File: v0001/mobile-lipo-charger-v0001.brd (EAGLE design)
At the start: 82.9 x 108.6 mm, 31 parts, among them IC2 STM32F401VBT, SW1 DHT-4235A

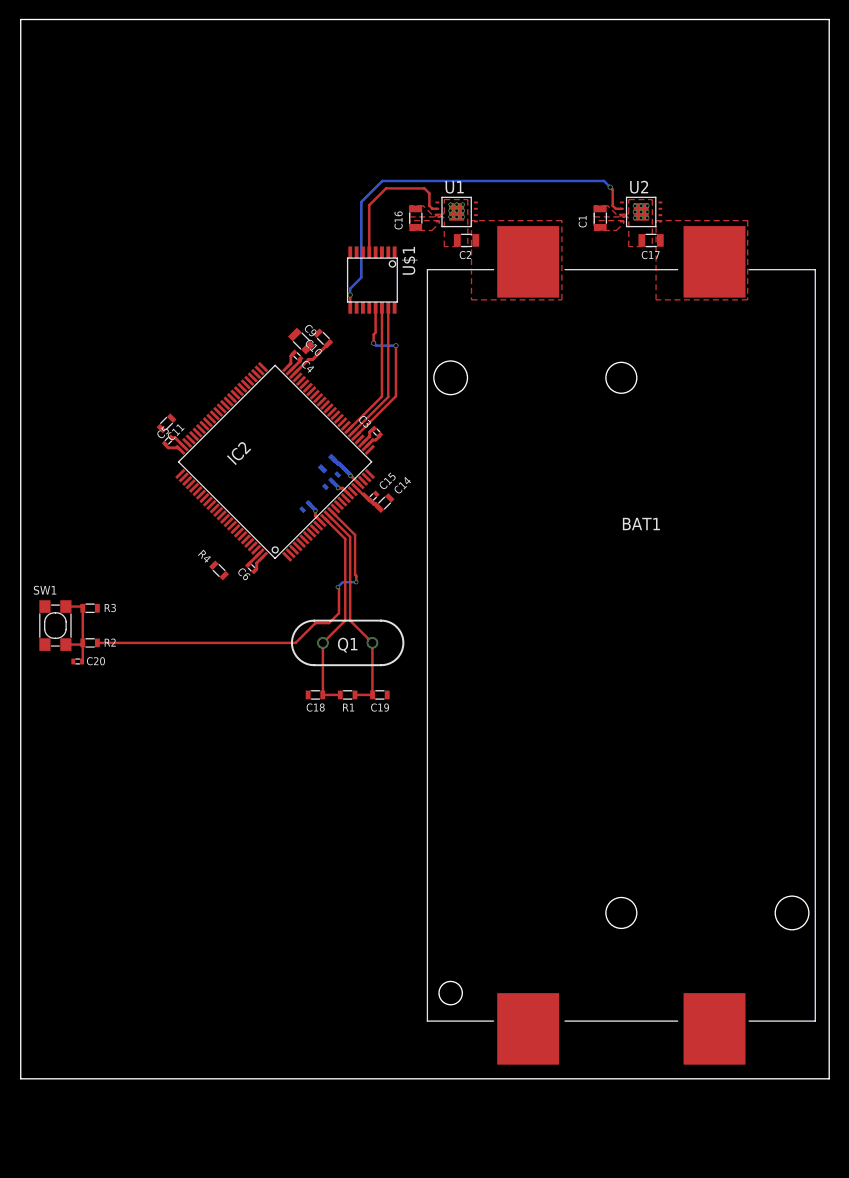
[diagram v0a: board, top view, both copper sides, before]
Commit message: Minor Changes
Made minor changes to the polygons for the charger chips
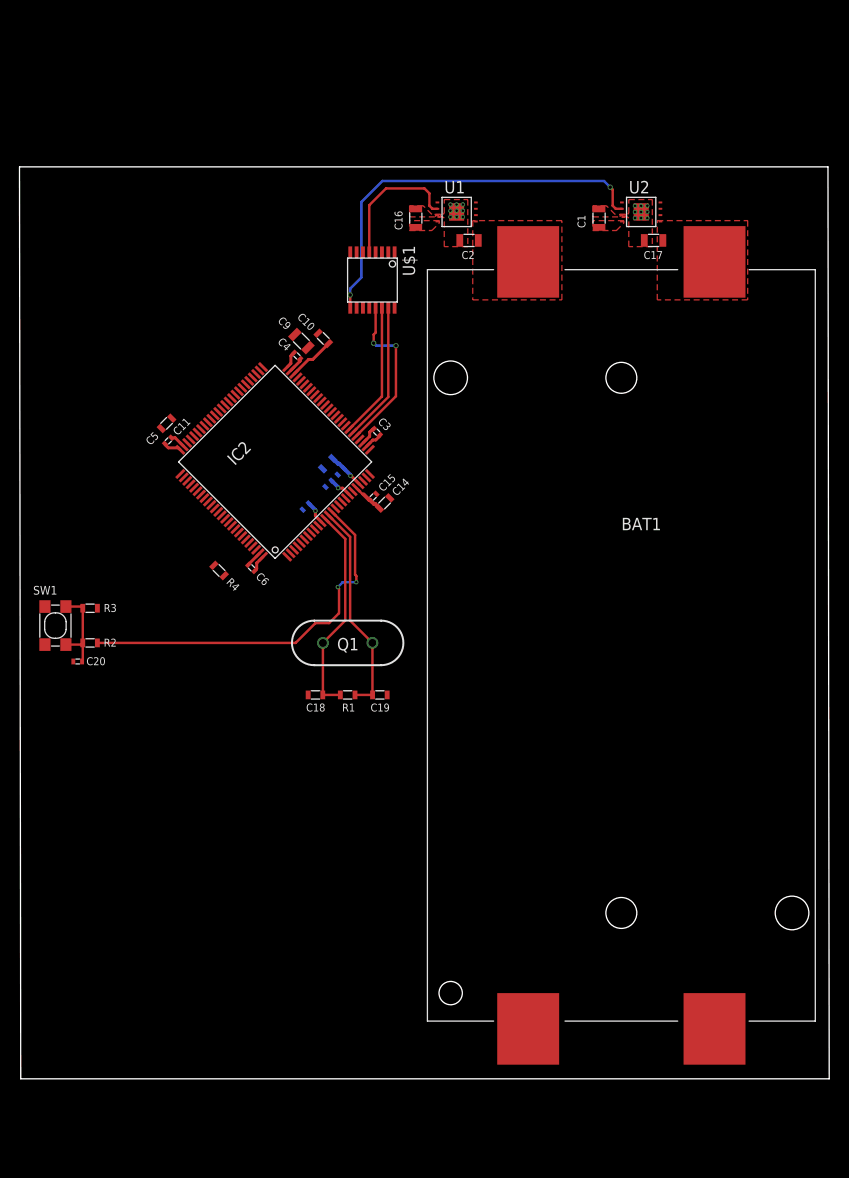
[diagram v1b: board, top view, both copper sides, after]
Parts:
- moved C17 0.25 mm to (64.9, 96.9)
- moved C2 0.25 mm to (46.0, 96.9)
- moved C1 0.13 mm to (59.3, 99.2)
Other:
- board size 82.9 x 108.6 mm -> 83 x 93.5 mm

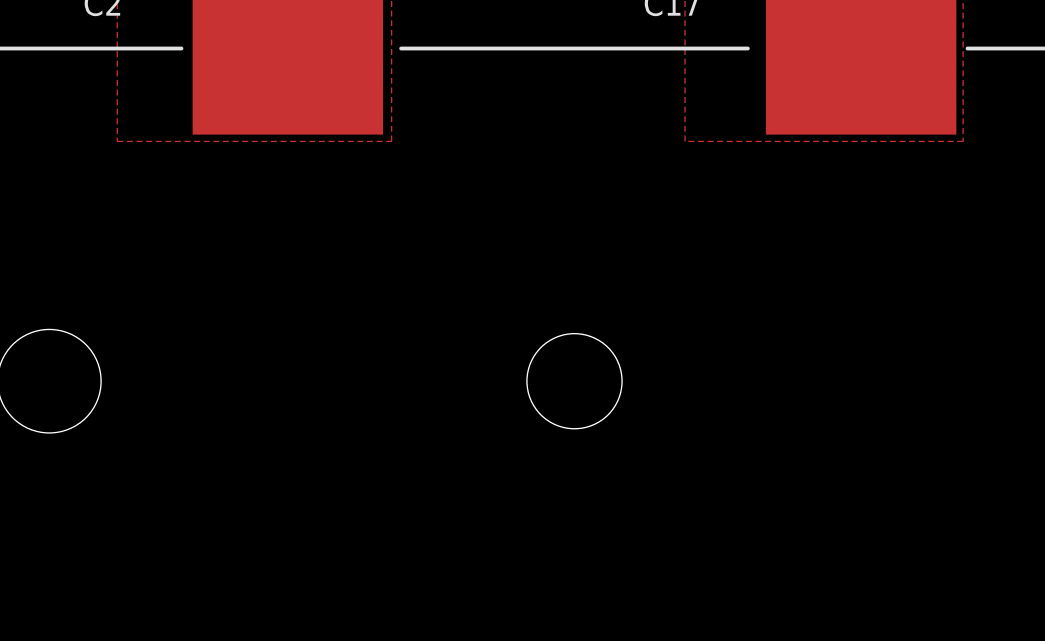
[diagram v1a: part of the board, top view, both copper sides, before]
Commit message: Added ADC Buffer
Added the ADC buffer and voltage divider for measuring the battery voltage before/during/after charging
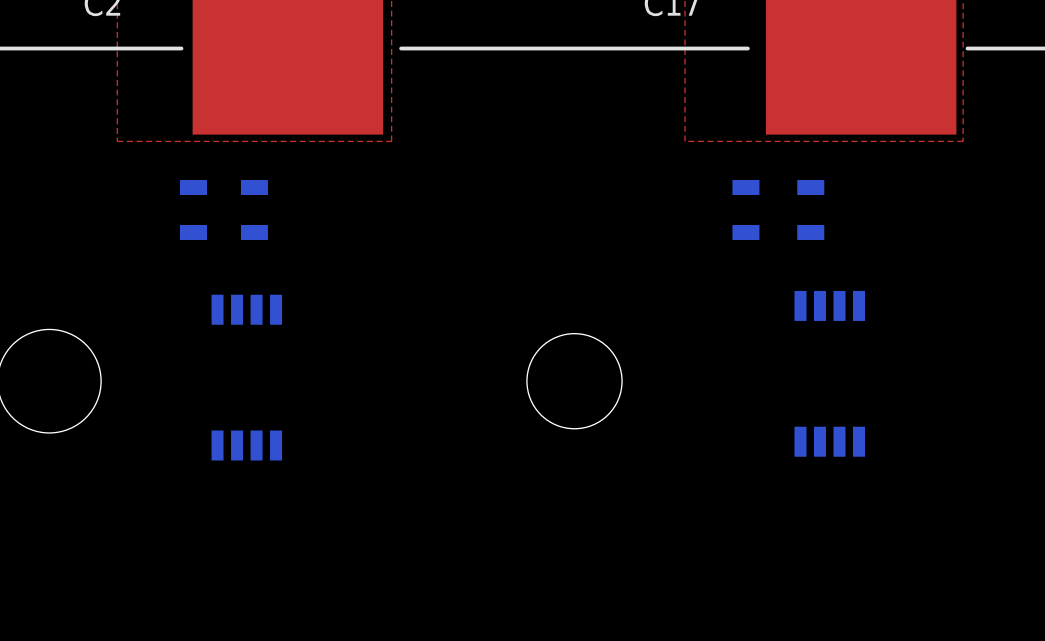
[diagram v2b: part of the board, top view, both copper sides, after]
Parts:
- added IC1, IC3: AD8610MR, analog-devices:MSOP08
- added R5, R7: 1.5k, common:0603L3
- added R6, R8: 5.49k, common:0603L3
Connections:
- new net ADC_BUFF1: IC1.3, R5.P$1, R6.P$2
- new net ADC_BUFF2: IC3.3, R7.P$1, R8.P$2
- new net BATT1_V: IC1.2, IC1.6, IC2.24
- new net BATT2_V: IC2.25, IC3.2, IC3.6
- new net N$8: IC3.7
- new net N$9: IC1.7
- net BATT1_OUT: now also R5.P$2
- net BATT2_OUT: now also R7.P$2
- net GND: now also IC1.4, IC3.4, R6.P$1, R8.P$1
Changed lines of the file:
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@@
 <layer number="17" name="Pads" color="2" fill="1" visible="yes" active="yes"/>
 <layer number="18" name="Vias" color="2" fill="1" visible="yes" active="yes"/>
-<layer number="19" name="Unrouted" color="6" fill="1" visible="no" active="yes"/>
+<layer number="19" name="Unrouted" color="6" fill="1" visible="yes" active="yes"/>
 <layer number="20" name="Dimension" color="24" fill="1" visible="yes" active="yes"/>
 <layer number="21" name="tPlace" color="7" fill="1" visible="yes" active="yes"/>
@@
 <attribute name="VALUE" x="61.595" y="63.754" size="1.27" layer="27"/>
 </element>
+<element name="R5" library="common" package="0603L3" value="1.5k" x="48.895" y="88.519" smashed="yes" rot="MR90">
+<attribute name="NAME" x="49.53" y="87.122" size="0.8128" layer="26" rot="MR90"/>
+<attribute name="VALUE" x="47.371" y="87.122" size="0.8128" layer="28" rot="MR90"/>
+</element>
+<element name="R6" library="common" package="0603L3" value="5.49k" x="50.927" y="88.519" smashed="yes" rot="MR270">
+<attribute name="NAME" x="50.292" y="89.916" size="0.8128" layer="26" rot="MR270"/>
+<attribute name="VALUE" x="52.451" y="89.916" size="0.8128" layer="28" rot="MR270"/>
+</element>
+<element name="R7" library="common" package="0603L3" value="1.5k" x="67.31" y="88.519" smashed="yes" rot="MR90">
+<attribute name="NAME" x="67.945" y="87.122" size="0.8128" layer="26" rot="MR90"/>
+<attribute name="VALUE" x="65.786" y="87.122" size="0.8128" layer="28" rot="MR90"/>
+</element>
+<element name="R8" library="common" package="0603L3" value="5.49k" x="69.469" y="88.519" smashed="yes" rot="MR270">
+<attribute name="NAME" x="68.834" y="89.916" size="0.8128" layer="26" rot="MR270"/>
+<attribute name="VALUE" x="70.993" y="89.916" size="0.8128" layer="28" rot="MR270"/>
+</element>
+<element name="IC1" library="analog-devices" library_urn="urn:adsk.eagle:library:102" package="MSOP08" package3d_urn="urn:adsk.eagle:package:3936/1" value="AD8610MR" x="50.673" y="82.931" smashed="yes" rot="MR180">
+<attribute name="MF" value="ALTERA CORPORATION" x="50.673" y="82.931" size="1.778" layer="28" rot="MR180" display="off"/>
+<attribute name="MPN" value="AD8610ARMZ-REEL" x="50.673" y="82.931" size="1.778" layer="28" rot="MR180" display="off"/>
+<attribute name="NAME" x="48.641" y="85.471" size="1.27" layer="26" ratio="10" rot="MR270"/>
+<attribute name="OC_FARNELL" value="1424175" x="50.673" y="82.931" size="1.778" layer="28" rot="MR180" display="off"/>
+<attribute name="OC_NEWARK" value="59K6939" x="50.673" y="82.931" size="1.778" layer="28" rot="MR180" display="off"/>
+<attribute name="POPULARITY" value="0" x="50.673" y="82.931" size="1.778" layer="28" rot="MR180" display="off"/>
+<attribute name="VALUE" x="53.975" y="85.471" size="1.27" layer="28" ratio="10" rot="MR270"/>
+</element>
+<element name="IC3" library="analog-devices" library_urn="urn:adsk.eagle:library:102" package="MSOP08" package3d_urn="urn:adsk.eagle:package:3936/1" value="AD8610MR" x="70.104" y="83.058" smashed="yes" rot="MR180">
+<attribute name="MF" value="ALTERA CORPORATION" x="70.104" y="83.058" size="1.778" layer="28" rot="MR180" display="off"/>
+<attribute name="MPN" value="AD8610ARMZ-REEL" x="70.104" y="83.058" size="1.778" layer="28" rot="MR180" display="off"/>
+<attribute name="NAME" x="68.072" y="85.598" size="1.27" layer="26" ratio="10" rot="MR270"/>
+<attribute name="OC_FARNELL" value="1424175" x="70.104" y="83.058" size="1.778" layer="28" rot="MR180" display="off"/>
+<attribute name="OC_NEWARK" value="59K6939" x="70.104" y="83.058" size="1.778" layer="28" rot="MR180" display="off"/>
+<attribute name="POPULARITY" value="0" x="70.104" y="83.058" size="1.778" layer="28" rot="MR180" display="off"/>
+<attribute name="VALUE" x="73.406" y="85.598" size="1.27" layer="28" ratio="10" rot="MR270"/>
+</element>
 </elements>
 <signals>
@@
 <vertex x="43.053" y="99.314"/>
 </polygon>
-<wire x1="37.043" y1="95.687" x2="36.393" y2="95.687" width="0" layer="19" extent="1-1"/>
+<contactref element="R6" pad="P$1"/>
+<contactref element="R8" pad="P$1"/>
+<contactref element="IC1" pad="4"/>
+<contactref element="IC3" pad="4"/>
+<wire x1="51.647" y1="85.194" x2="50.927" y2="89.269" width="0" layer="19" extent="16-16"/>
+<wire x1="45.024" y1="96.901" x2="50.927" y2="89.269" width="0" layer="19" extent="1-16"/>
+<wire x1="37.043" y1="95.687" x2="40.513" y2="100.137" width="0" layer="19" extent="1-1"/>
+<wire x1="36.393" y1="95.687" x2="37.043" y2="95.687" width="0" layer="19" extent="1-1"/>
 <wire x1="34.443" y1="95.687" x2="36.393" y2="95.687" width="0" layer="19" extent="1-1"/>
 <wire x1="33.793" y1="95.687" x2="34.443" y2="95.687" width="0" layer="19" extent="1-1"/>
-<wire x1="40.513" y1="100.137" x2="37.043" y2="95.687" width="0" layer="19" extent="1-1"/>
 <wire x1="30.496415625" y1="87.382275" x2="33.793" y2="95.687" width="0" layer="19" extent="1-1"/>
 <wire x1="29.453434375" y1="85.910784375" x2="30.496415625" y2="87.382275" width="0" layer="19" extent="1-1"/>
@@
 <wire x1="16.7184375" y1="75.780771875" x2="27.678590625" y2="83.558946875" width="0" layer="19" extent="1-1"/>
 <wire x1="14.421759375" y1="77.610765625" x2="15.449890625" y2="76.66324375" width="0" layer="19" extent="1-1"/>
-<wire x1="59.309" y1="100.137" x2="45.339" y2="100.584" width="0" layer="19" extent="1-1"/>
+<wire x1="59.309" y1="100.137" x2="50.927" y2="89.269" width="0" layer="19" extent="1-16"/>
 <wire x1="29.476" y1="50.292" x2="23.3447375" y2="63.641871875" width="0" layer="19" extent="1-1"/>
 <wire x1="37.58" y1="50.292" x2="29.476" y2="50.292" width="0" layer="19" extent="1-1"/>
@@
 <wire x1="52.04" y1="16.042" x2="37.58" y2="50.292" width="0" layer="19" extent="1-1"/>
 <wire x1="71.15" y1="16.042" x2="52.04" y2="16.042" width="0" layer="19" extent="1-1"/>
+<wire x1="69.469" y1="89.269" x2="52.04" y2="16.042" width="0" layer="19" extent="1-16"/>
+<wire x1="71.078" y1="85.321" x2="69.469" y2="89.269" width="0" layer="19" extent="16-16"/>
 </signal>
 <signal name="BATT+">
@@
 </polygon>
 <contactref element="BAT1" pad="1"/>
+<contactref element="R5" pad="P$2"/>
+<wire x1="52.04" y1="94.702" x2="48.895" y2="89.269" width="0" layer="19" extent="1-16"/>
 </signal>
 <signal name="BATT1_CE">
@@
 </polygon>
 <contactref element="BAT1" pad="4"/>
+<contactref element="R7" pad="P$2"/>
+<wire x1="71.15" y1="94.702" x2="67.31" y2="89.269" width="0" layer="19" extent="1-16"/>
 </signal>
 <signal name="BATT2_ISET">
@@
 <wire x1="19.809909375" y1="63.584596875" x2="22.72884375" y2="66.588384375" width="0" layer="19" extent="1-1"/>
 </signal>
+<signal name="BATT1_V">
+<contactref element="IC2" pad="24"/>
+<contactref element="IC1" pad="6"/>
+<contactref element="IC1" pad="2"/>
+<wire x1="50.997" y1="80.669" x2="50.347" y2="85.194" width="0" layer="19" extent="16-16"/>
+<wire x1="35.456765625" y1="72.59879375" x2="50.997" y2="80.669" width="0" layer="19" extent="1-16"/>
+</signal>
+<signal name="BATT2_V">
+<contactref element="IC2" pad="25"/>
+<contactref element="IC3" pad="6"/>
+<contactref element="IC3" pad="2"/>
+<wire x1="70.428" y1="80.796" x2="35.81031875" y2="72.952346875" width="0" layer="19" extent="1-16"/>
+<wire x1="69.778" y1="85.321" x2="70.428" y2="80.796" width="0" layer="19" extent="16-16"/>
+</signal>
+<signal name="ADC_BUFF1">
+<contactref element="R5" pad="P$1"/>
+<contactref element="R6" pad="P$2"/>
+<contactref element="IC1" pad="3"/>
+<wire x1="48.895" y1="87.769" x2="50.927" y2="87.769" width="0" layer="19" extent="16-16"/>
+<wire x1="50.997" y1="85.194" x2="50.927" y2="87.769" width="0" layer="19" extent="16-16"/>
+</signal>
+<signal name="ADC_BUFF2">
+<contactref element="R8" pad="P$2"/>
+<contactref element="R7" pad="P$1"/>
+<contactref element="IC3" pad="3"/>
+<wire x1="69.469" y1="87.769" x2="67.31" y2="87.769" width="0" layer="19" extent="16-16"/>
+<wire x1="70.428" y1="85.321" x2="69.469" y2="87.769" width="0" layer="19" extent="16-16"/>
+</signal>
+<signal name="N$8">
+<contactref element="IC3" pad="7"/>
+</signal>
+<signal name="N$9">
+<contactref element="IC1" pad="7"/>
+</signal>
 </signals>

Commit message: Added buffers
Added the buffers to the ADC for the MCU and laid out the board for those parts.
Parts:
- added JP1: (no value), pinhead:2X05
- moved R7 1.02 mm to (68.3, 88.5)
- moved R8 0.89 mm to (70.4, 88.5)
- moved IC3 0.13 mm to (70.1, 82.9)
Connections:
- new net TCK_SWCLK: IC2.76, JP1.4
- new net TMS_SWDIO: IC2.72, JP1.2
- net BATT1_V: now also IC2.25; no longer IC2.24
- net BATT2_V: now also IC2.24; no longer IC2.25
- net GND: now also JP1.3, JP1.5, JP1.9
- net RST: now also JP1.10
- net VDD: now also JP1.1
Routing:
- net RST: track 39.1 -> 85.2 mm
- net BATT2_V: track 0.00 -> 45.5 mm, vias 0 -> 1
- net TCK_SWCLK: track 0.00 -> 32.1 mm
- net BATT1_V: track 0.00 -> 26.7 mm, vias 0 -> 1
- net TMS_SWDIO: track 0.00 -> 24.7 mm
- net GND: track 6.76 -> 11.6 mm
- net ADC_BUFF2: track 0.00 -> 4.64 mm
- net ADC_BUFF1: track 0.00 -> 4.64 mm
- net VCAP2: track 0.00 -> 3.20 mm
- net VDD: track 16.2 -> 18.7 mm
- net BATT2_OUT: track 0.00 -> 2.04 mm, vias 0 -> 1
- net BATT1_OUT: track 0.00 -> 2.04 mm, vias 0 -> 1
